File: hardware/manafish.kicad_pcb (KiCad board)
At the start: 4 copper layers, 70 x 100 mm, 103 parts, among them IC1 TPD4EUSB30, IC10 WSEN-PADS_2511020213301, IC11 BMI270, IC12 SHT45-AD1F-R2, IC2 TPD4EUSB30, IC3 JXF0-1012NL, IC4 RP2354A, IC5 Ag59824-LPB, IC6 LTV-817S, IC7 LTV-817S, IC8 LTC4162-LAD, IC9 TPSM53603RDA, J1 Conn_01x04_Pin, J2 SM03B-SRSS-TB, J3 AM32_1, J4 AM32_2, J5 Conn_01x22_Female, J6 Battery, J7 Conn_02x07_Odd_Even, J8 USB_C_Receptacle_USB2.0_14P, J9 Conn_02x08_Odd_Even, Q1 FDMC8327L, Q2 FDMC8327L, Y1 ABM8-272-T3

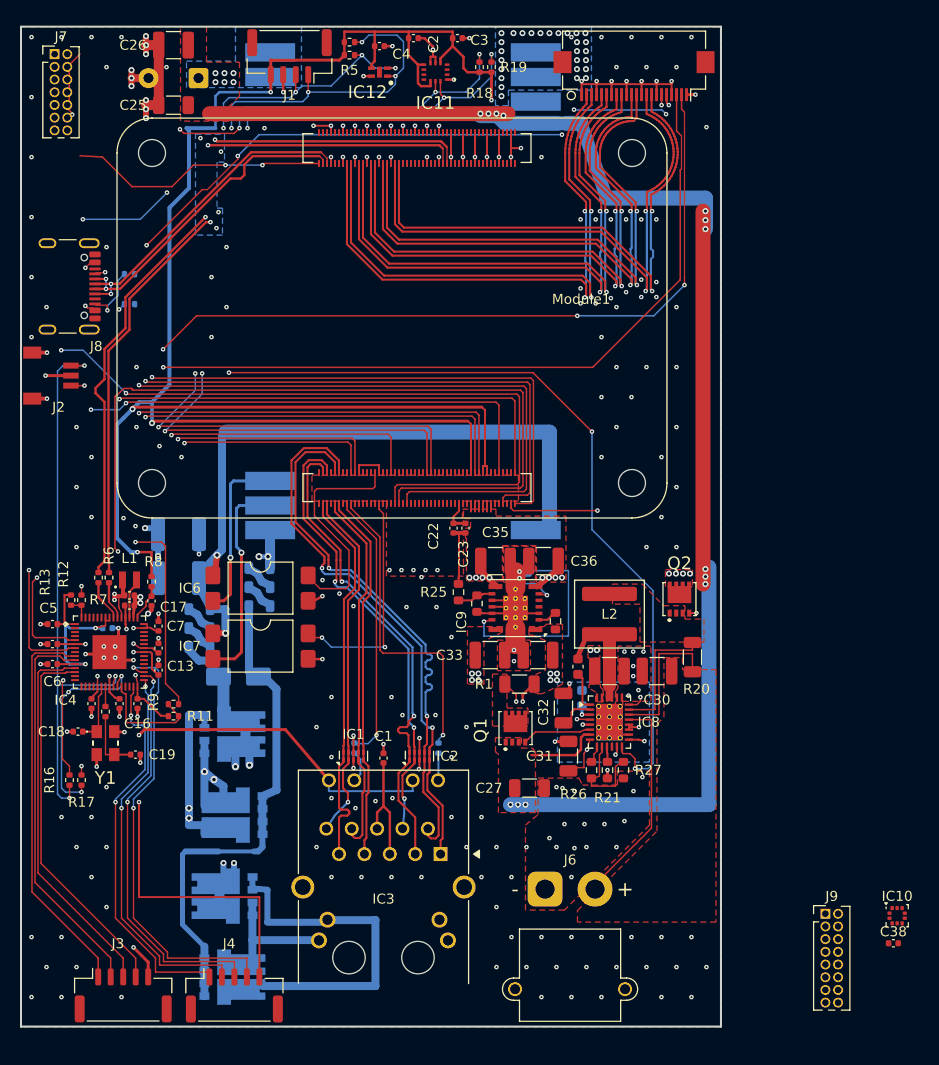
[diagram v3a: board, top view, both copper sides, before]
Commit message: Redo the PCB layout: 70 x 90 mm, power section grouped, one-side reflow
- Second camera connector J11 beside J5 on the top edge.
- SHT45 on a slotted tongue (no pour, no vias, four tracks over a 2.5 mm
  bridge) for thermal decoupling.
- All fine-pitch parts on top; the bottom holds only hand-solderable parts
  (IC5, connectors, 0603+ passives, fuses, electrolytics).
- MagJack, PoE module, charger, 5 V buck and battery connector grouped in
  the bottom half.
- Four M2 mounting holes H1-H4; silkscreen labels for the connectors and
  pin tables for J7, J9 and J13 on the bottom.
- Header pins remapped to simplify routing: J9 (CM5 GPIO), J13 (RP2354A
  GPIO22-29) and J7 (CM5 config); schematic labels updated to match.
- Default clearance 0.1 mm; DRC rules for C20's thermal, top parts under the
  CM5, IC10's land pattern and the edge parts.
- DRC: 0 errors, schematic parity clean; one expected unconnected item
  (CM5 connector-A GND pin 7, tied inside the CM5).

Co-Authored-By: Claude Opus 5.5 <noreply@anthropic.com>
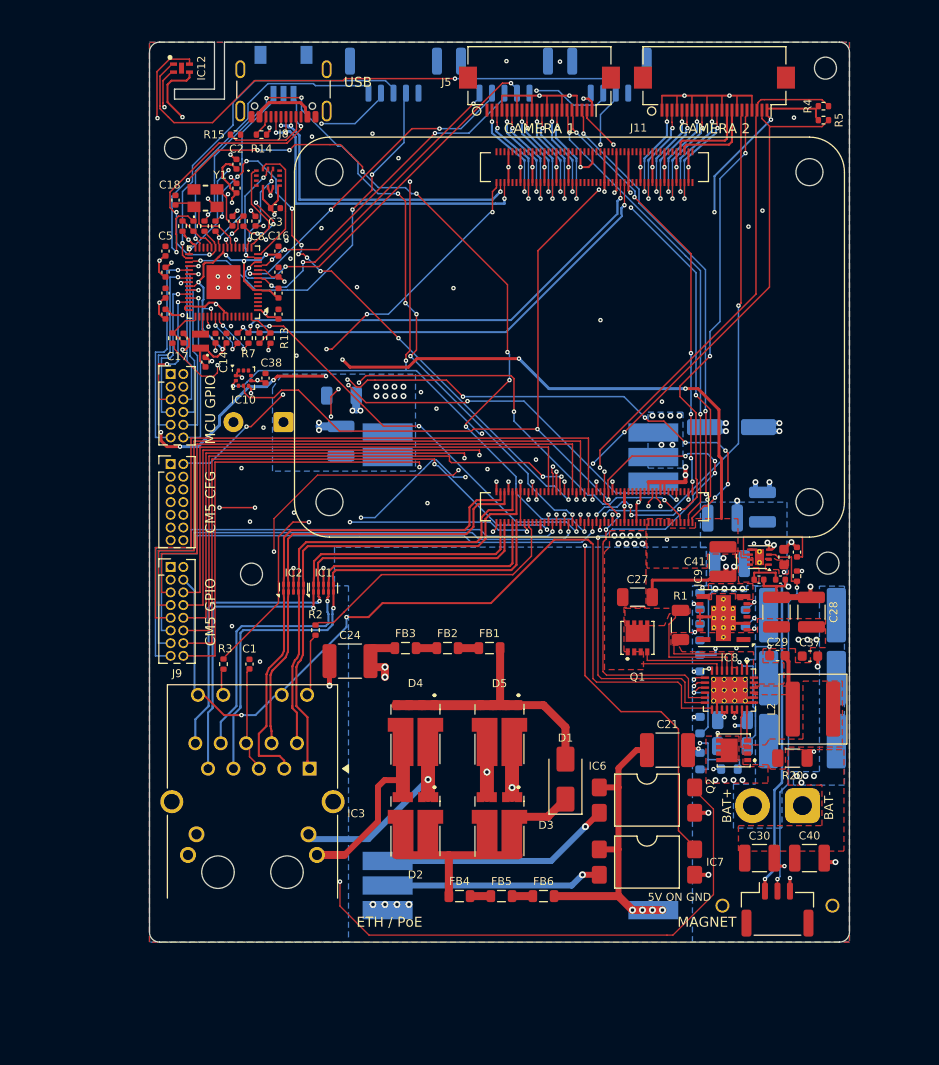
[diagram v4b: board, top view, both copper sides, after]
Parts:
- removed R18, R19: 4.7kR, Resistor_SMD:R_0402_1005Metric
- added C39: 47uF 35V, Capacitor_SMD:CP_Elec_6.3x5.8, B.Cu at (158.2, 88.5)
- added C40: 10uF 50V, Capacitor_SMD:C_1210_3225Metric, F.Cu at (166.0, 131.6)
- added C41: 47uF 10V, Capacitor_SMD:C_1210_3225Metric, F.Cu at (157.3, 102.0)
- added C47: 10uF, Capacitor_SMD:C_0603_1608Metric, F.Cu at (163.4, 101.5)
- added C48: 10nF 50V, Capacitor_SMD:C_0402_1005Metric, F.Cu at (164.8, 101.0)
- added F1: MF-LSMF260/33X-2, Fuse:Fuse_2920_7451Metric, B.Cu at (165.3, 107.3)
- added F2: MF-LSMF260/33X-2, Fuse:Fuse_2920_7451Metric, B.Cu at (165.3, 113.6)
- added F3: MF-LSMF260/33X-2, Fuse:Fuse_2920_7451Metric, B.Cu at (165.3, 119.9)
- added H1: MountingHole_2.2mm_M2, MountingHole_2.2mm_M2, F.Cu at (167.6, 52.6)
- added H2: MountingHole_2.2mm_M2, MountingHole_2.2mm_M2, F.Cu at (102.6, 60.6)
- added H3: MountingHole_2.2mm_M2, MountingHole_2.2mm_M2, F.Cu at (110.2, 103.2)
- added H4: MountingHole_2.2mm_M2, MountingHole_2.2mm_M2, F.Cu at (167.9, 102.1)
- added IC15: TPS22965DSGR, Package_SON:Texas_DSG0008A_WSON-8-1EP_2x2mm_P0.5mm_EP0.9x1.6mm_ThermalVias, F.Cu at (161.0, 101.5)
- added J11: Conn_01x22_Female, CM5IO:Hirose_FH12-22S-0.5SH_1x22-1MP_P0.50mm_Horizontal, F.Cu at (156.5, 55.0)
- added J12: Magnet, Connector_JST:JST_GH_SM03B-GHS-TB_1x03-1MP_P1.25mm_Horizontal, F.Cu at (162.8, 136.8)
- added J13: Conn_02x06_Odd_Even, Connector_PinHeader_1.27mm:PinHeader_2x06_P1.27mm_Vertical, F.Cu at (102.1, 83.2)
- added R29: 100kR, Resistor_SMD:R_0402_1005Metric, F.Cu at (164.8, 103.4)
- C11, C21, C24, C37, D1, D2, D3, D4, D5, FB1, FB2, FB3, FB4, FB5, FB6, R14, R15, R2, R3: moved to F.Cu
- C25, C26, C31, C32, C34, C35, C36, J1, J2, J3, J4, J6, R21, R22, R25, R26, R27: moved to B.Cu
- IC9: value TPSM53603RDA -> TPSM53604RDA
- R1: value 16mR -> 8mR
- R24: value 2.49kR -> 2.43kR; moved to B.Cu
- R4, R5: value 4.7kR -> 2.2kR
- moved J3 99.7 mm to (135.5, 53.2)
- moved J4 93.5 mm to (124.4, 53.2)
- moved IC10 84.6 mm to (109.4, 83.6)
- moved C38 84.5 mm to (111.6, 83.6), turned to 90 degrees
- moved J9 74.1 mm to (102.1, 102.5)
- moved R16 57.3 mm to (106.6, 68.4)
- moved R17 56.7 mm to (105.5, 68.4)
- moved Y1 55.4 mm to (105.6, 65.6), turned to 0 degrees
- moved C19 54.2 mm to (108.3, 67.9), turned to 90 degrees
- moved C18 54.0 mm to (102.6, 65.8), turned to 90 degrees
- moved C21 51.8 mm to (151.8, 120.8), turned to 0 degrees
- moved R10 51.0 mm to (109.4, 67.9)
- moved R11 49.0 mm to (103.3, 68.4), turned to 90 degrees
- moved R5 48.0 mm to (167.4, 57.8)
- moved C16 48.0 mm to (112.9, 70.9), turned to 90 degrees
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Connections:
- net /Camera Serial Interface/CAM_GPIO0 renamed /Camera Serial Interface/CAM0_GPIO0
- net /Camera Serial Interface/CAM_GPIO1 renamed /Camera Serial Interface/CAM0_GPIO1
- net /RP2354A/VREG_FB renamed /RP2354A/+1.1V
- C10 pad 1: /RP2354A/VREG_VIN -> /RP2354A/+3.3V
- C11 pad 1: /RP2354A/VREG_VIN -> /RP2354A/+3.3V
- C15 pad 1: /RP2354A/VREG_VIN -> /RP2354A/+3.3V
- C2 pad 1: /RP2354A/VREG_VIN -> /RP2354A/+3.3V
- C22 pad 1: /Power Management/+5V -> /+5V
- C23 pad 1: /Power Management/+5V -> /+5V
- C3 pad 1: /RP2354A/VREG_VIN -> /RP2354A/+3.3V
- C35 pad 1: /Power Management/+5V -> /Power Management/+5V_AON
- C36 pad 1: /Power Management/+5V -> /Power Management/+5V_AON
- C38 pad 1: /RP2354A/VREG_VIN -> /RP2354A/+3.3V
- C4 pad 1: /RP2354A/VREG_VIN -> /RP2354A/+3.3V
- C5 pad 1: /RP2354A/VREG_VIN -> /RP2354A/+3.3V
- C6 pad 1: /RP2354A/VREG_VIN -> /RP2354A/+3.3V
- C7 pad 1: /RP2354A/VREG_VIN -> /RP2354A/+3.3V
- C8 pad 1: /RP2354A/VREG_VIN -> /RP2354A/+3.3V
- C9 pad 1: /RP2354A/VREG_VIN -> /RP2354A/+3.3V
- IC10 pad 1: /RP2354A/VREG_VIN -> /RP2354A/+3.3V
- IC10 pad 10: /RP2354A/VREG_VIN -> /RP2354A/+3.3V
- IC10 pad 2: /I2C Peripherals/I2C1_SCL -> /Power Management/I2C1_SCL
- IC10 pad 4: /I2C Peripherals/I2C1_SDA -> /Power Management/I2C1_SDA
- IC10 pad 5: unconnected-(U10-SA0-Pad5) -> GND
- IC10 pad 6: unconnected-(U10-~{CS}-Pad6) -> /RP2354A/+3.3V
- IC10 pad 7: /I2C Peripherals/INT_DRDY -> unconnected-(IC10-INT_DRDY-Pad7)
- IC11 pad 1: GND -> /RP2354A/MISO
- IC11 pad 12: /RP2354A/VREG_VIN -> /RP2354A/CS
- IC11 pad 13: /I2C Peripherals/I2C0_SCL -> /RP2354A/SCK
- IC11 pad 14: /I2C Peripherals/I2C0_SDA -> /RP2354A/MOSI
- IC11 pad 5: /RP2354A/VREG_VIN -> /RP2354A/+3.3V
- IC11 pad 8: /RP2354A/VREG_VIN -> /RP2354A/+3.3V
- IC12 pad 1: /I2C Peripherals/I2C1_SDA -> /Power Management/I2C1_SDA
- IC12 pad 2: /I2C Peripherals/I2C1_SCL -> /Power Management/I2C1_SCL
- IC12 pad 3: /RP2354A/VREG_VIN -> /RP2354A/+3.3V
- IC3 pad 11: /RP2354A/VREG_VIN -> /RP2354A/+3.3V
- IC3 pad 13: /RP2354A/VREG_VIN -> /RP2354A/+3.3V
- IC4 pad 1: /RP2354A/VREG_VIN -> /RP2354A/+3.3V
- IC4 pad 11: /RP2354A/VREG_VIN -> /RP2354A/+3.3V
- IC4 pad 14: unconnected-(U4-GPIO10-Pad14) -> /RP2354A/SCK
- IC4 pad 15: unconnected-(U4-GPIO11-Pad15) -> /RP2354A/MOSI
- IC4 pad 16: unconnected-(U4-GPIO12-Pad16) -> /RP2354A/MISO
- IC4 pad 17: unconnected-(U4-GPIO13-Pad17) -> /RP2354A/CS
- IC4 pad 20: /RP2354A/VREG_VIN -> /RP2354A/+3.3V
- IC4 pad 30: /RP2354A/VREG_VIN -> /RP2354A/+3.3V
- IC4 pad 34: unconnected-(U4-GPIO22-Pad34) -> /RP2354A/GPIO22
- IC4 pad 35: unconnected-(U4-GPIO23-Pad35) -> /RP2354A/GPIO23
- IC4 pad 36: unconnected-(U4-GPIO24-Pad36) -> /RP2354A/GPIO24
- IC4 pad 37: unconnected-(U4-GPIO25-Pad37) -> /RP2354A/GPIO25
- IC4 pad 38: /RP2354A/VREG_VIN -> /RP2354A/+3.3V
- IC4 pad 40: unconnected-(U4-GPIO26/ADC0-Pad40) -> /RP2354A/GPIO26
- IC4 pad 41: unconnected-(U4-GPIO27/ADC1-Pad41) -> /RP2354A/GPIO27
- IC4 pad 42: unconnected-(U4-GPIO28/ADC2-Pad42) -> /RP2354A/GPIO28
- IC4 pad 43: unconnected-(U4-GPIO29/ADC3-Pad43) -> /RP2354A/GPIO29
- IC4 pad 44: /RP2354A/VREG_VIN -> /RP2354A/+3.3V
- IC4 pad 45: /RP2354A/VREG_VIN -> /RP2354A/+3.3V
- IC4 pad 49: /RP2354A/VREG_VIN -> /RP2354A/+3.3V
- IC4 pad 5: /I2C Peripherals/I2C0_SCL -> unconnected-(IC4-GPIO3-Pad5)
- IC4 pad 53: /RP2354A/VREG_VIN -> /RP2354A/+3.3V
- IC4 pad 54: /RP2354A/VREG_VIN -> /RP2354A/+3.3V
- IC4 pad 7: /I2C Peripherals/I2C0_SDA -> unconnected-(IC4-GPIO4-Pad7)
- IC8 pad 13: /I2C Peripherals/I2C1_SCL -> /Power Management/I2C1_SCL
- IC8 pad 14: /I2C Peripherals/I2C1_SDA -> /Power Management/I2C1_SDA
- IC8 pad 15: /RP2354A/VREG_VIN -> /RP2354A/+3.3V
- IC9 pad 7: /Power Management/+5V -> /Power Management/+5V_AON
- IC9 pad 8: /Power Management/+5V -> /Power Management/+5V_AON
- J1 pad 1: /I2C Peripherals/I2C1_SDA -> /RP2354A/+3.3V
- J1 pad 2: /I2C Peripherals/I2C1_SCL -> /Power Management/I2C1_SCL
- J1 pad 3: GND -> /Power Management/I2C1_SDA
- J1 pad 4: /RP2354A/VREG_VIN -> GND
- J5 pad 22: /RP2354A/VREG_VIN -> /RP2354A/+3.3V
- J6 pad 2: /Power Management/BAT+ -> /BAT_IN
- J7 pad 10: /Rasperry Pi Compute Module 5/USBOTG -> /Rasperry Pi Compute Module 5/nRPIBOOT
- J7 pad 12: /Rasperry Pi Compute Module 5/PMIC_ENABLE -> /Rasperry Pi Compute Module 5/EEPROM_nWP
- J7 pad 14: /Rasperry Pi Compute Module 5/PWR_BUT -> /Rasperry Pi Compute Module 5/SYNC_OUT
- J7 pad 2: /Rasperry Pi Compute Module 5/nRPIBOOT -> /Rasperry Pi Compute Module 5/USBOTG
- J7 pad 4: /Rasperry Pi Compute Module 5/EEPROM_nWP -> /Rasperry Pi Compute Module 5/PWR_BUT
- J7 pad 6: /Rasperry Pi Compute Module 5/SYNC_OUT -> /Rasperry Pi Compute Module 5/PMIC_ENABLE
- J9 pad 1: /Rasperry Pi Compute Module 5/GPIO21 -> /+5V
- J9 pad 11: /Rasperry Pi Compute Module 5/GPIO23 -> /Rasperry Pi Compute Module 5/GPIO18
- J9 pad 12: /Rasperry Pi Compute Module 5/GPIO27 -> /Rasperry Pi Compute Module 5/GPIO5
- J9 pad 13: /Rasperry Pi Compute Module 5/GPIO18 -> /Rasperry Pi Compute Module 5/GPIO7
- J9 pad 14: /Rasperry Pi Compute Module 5/GPIO17 -> /Rasperry Pi Compute Module 5/GPIO23
- J9 pad 15: /Rasperry Pi Compute Module 5/GPIO15 -> /Rasperry Pi Compute Module 5/GPIO16
- J9 pad 16: /Rasperry Pi Compute Module 5/GPIO4 -> /Rasperry Pi Compute Module 5/GPIO20
- J9 pad 2: /Rasperry Pi Compute Module 5/GPIO19 -> GND
- J9 pad 3: /Rasperry Pi Compute Module 5/GPIO20 -> GND
- J9 pad 4: /Rasperry Pi Compute Module 5/GPIO13 -> /RP2354A/+3.3V
- J9 pad 5: /Rasperry Pi Compute Module 5/GPIO16 -> /Rasperry Pi Compute Module 5/GPIO9
- J9 pad 6: /Rasperry Pi Compute Module 5/GPIO5 -> /Rasperry Pi Compute Module 5/GPIO13
- J9 pad 7: /Rasperry Pi Compute Module 5/GPIO7 -> /Rasperry Pi Compute Module 5/GPIO10
- J9 pad 8: /Rasperry Pi Compute Module 5/GPIO9 -> /Rasperry Pi Compute Module 5/GPIO17
- J9 pad 9: /Rasperry Pi Compute Module 5/GPIO10 -> /Rasperry Pi Compute Module 5/GPIO27
- Module1 pad 175: unconnected-(Module1B-MIPI1_D0_N-Pad175) -> /Camera Serial Interface/DPHY1_D0_N
- Module1 pad 177: unconnected-(Module1B-MIPI1_D0_P-Pad177) -> /Camera Serial Interface/DPHY1_D0_P
- Module1 pad 181: unconnected-(Module1B-MIPI1_D1_N-Pad181) -> /Camera Serial Interface/DPHY1_D1_N
- Module1 pad 183: unconnected-(Module1B-MIPI1_D1_P-Pad183) -> /Camera Serial Interface/DPHY1_D1_P
- Module1 pad 187: unconnected-(Module1B-MIPI1_C_N-Pad187) -> /Camera Serial Interface/DPHY1_C_N
- Module1 pad 189: unconnected-(Module1B-MIPI1_C_P-Pad189) -> /Camera Serial Interface/DPHY1_C_P
- Module1 pad 193: unconnected-(Module1B-MIPI1_D2_N-Pad193) -> /Camera Serial Interface/DPHY1_D2_N
- Module1 pad 194: unconnected-(Module1B-MIPI1_D3_N-Pad194) -> /Camera Serial Interface/DPHY1_D3_N
- Module1 pad 195: unconnected-(Module1B-MIPI1_D2_P-Pad195) -> /Camera Serial Interface/DPHY1_D2_P
- Module1 pad 196: unconnected-(Module1B-MIPI1_D3_P-Pad196) -> /Camera Serial Interface/DPHY1_D3_P
- Module1 pad 24: /I2C Peripherals/INT_DRDY -> unconnected-(Module1A-GPIO26-Pad24)
- Module1 pad 25: /Rasperry Pi Compute Module 5/GPIO21 -> unconnected-(Module1A-GPIO21-Pad25)
- Module1 pad 26: /Rasperry Pi Compute Module 5/GPIO19 -> unconnected-(Module1A-GPIO19-Pad26)
- Module1 pad 35: unconnected-(Module1A-ID_SC-Pad35) -> /Camera Serial Interface/SCL1
- Module1 pad 36: unconnected-(Module1A-ID_SD-Pad36) -> /Camera Serial Interface/SDA1
- Module1 pad 51: /Rasperry Pi Compute Module 5/GPIO15 -> /Camera Serial Interface/CAM1_GPIO1
- Module1 pad 54: /Rasperry Pi Compute Module 5/GPIO4 -> unconnected-(Module1A-GPIO4-Pad54)
- Module1 pad 55: unconnected-(Module1A-GPIO14-Pad55) -> /Camera Serial Interface/CAM1_GPIO0
- Module1 pad 56: /I2C Peripherals/I2C1_SCL -> /Power Management/I2C1_SCL
- Module1 pad 58: /I2C Peripherals/I2C1_SDA -> /Power Management/I2C1_SDA
- Module1 pad 77: /Power Management/+5V -> /+5V
- Module1 pad 78: /RP2354A/VREG_VIN -> /RP2354A/+3.3V
- Module1 pad 79: /Power Management/+5V -> /+5V
- Module1 pad 81: /Power Management/+5V -> /+5V
- Module1 pad 83: /Power Management/+5V -> /+5V
- Module1 pad 84: /RP2354A/VREG_VIN -> /RP2354A/+3.3V
- Module1 pad 85: /Power Management/+5V -> /+5V
- Module1 pad 86: /RP2354A/VREG_VIN -> /RP2354A/+3.3V
- Module1 pad 87: /Power Management/+5V -> /+5V
- R11 pad 1: /RP2354A/VREG_VIN -> /RP2354A/+3.3V
- R13 pad 1: /RP2354A/VREG_VIN -> /RP2354A/+3.3V
- R25 pad 1: /Power Management/+5V -> /Power Management/+5V_AON
- R4 pad 1: /RP2354A/VREG_VIN -> /RP2354A/+3.3V
- R4 pad 2: /I2C Peripherals/I2C1_SCL -> /Camera Serial Interface/SCL1
- R5 pad 1: /RP2354A/VREG_VIN -> /RP2354A/+3.3V
- R5 pad 2: /I2C Peripherals/I2C1_SDA -> /Camera Serial Interface/SDA1
- R8 pad 1: /RP2354A/VREG_VIN -> /RP2354A/+3.3V
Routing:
- net /RP2354A/VREG_VIN: track 316.9 -> 0.00 mm, vias 16 -> 0
- net /I2C Peripherals/I2C1_SCL: track 199.9 -> 0.00 mm, vias 9 -> 0
- net /RP2354A/+3.3V: track 0.00 -> 194.1 mm, vias 0 -> 25
- net /Power Management/I2C1_SDA: track 0.00 -> 186.0 mm, vias 0 -> 9
- net /I2C Peripherals/I2C1_SDA: track 183.1 -> 0.00 mm, vias 9 -> 0
- net /Power Management/I2C1_SCL: track 0.00 -> 152.4 mm, vias 0 -> 9
- net /Power Management/24V: track 149.4 -> 7.94 mm, vias 19 -> 16
- net /I2C Peripherals/I2C0_SDA: track 117.1 -> 0.00 mm, vias 4 -> 0
- net /Power Management/POE_TYP2_DET: track 22.4 -> 127.2 mm, vias 0 -> 4
- net /I2C Peripherals/I2C0_SCL: track 102.3 -> 0.00 mm, vias 7 -> 0
- net /+5V: track 0.00 -> 100.0 mm, vias 0 -> 7
- net /Camera Serial Interface/CAM0_GPIO1: track 125.1 -> 42.2 mm, vias 5 -> 6
- net /Camera Serial Interface/SDA0: track 121.5 -> 49.9 mm, vias 4 -> 5
- net /Rasperry Pi Compute Module 5/GPIO27: track 0.00 -> 68.1 mm
- net /Camera Serial Interface/SCL0: track 118.3 -> 50.4 mm, vias 2 -> 4
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- added copper zone on F.Cu, net /+5V
- added copper zone on B.Cu, net /BAT_IN
- added copper zone on B.Cu, net /Power Management/+5V_AON
- added copper zone on F.Cu, net /Power Management/+5V_AON
- added copper zone on In2.Cu, net /Power Management/24V
- added copper zone on B.Cu, net /Power Management/BAT+
- added copper zone on In2.Cu, net /RP2354A/+3.3V
- added copper zone on F.Cu, net Net-(C29-Pad2)
- removed copper zone on F.Cu, net /Power Management/+5V
- removed copper zone on In2.Cu, net /Power Management/+5V
- removed copper zone on In2.Cu, net /RP2354A/VREG_VIN
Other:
- board size 70 x 100 mm -> 70 x 90 mm
- board text added: "1 5V"
- board text added: "1 GND"
- board text added: "10 GP26"
- board text added: "10 IO22"
- board text added: "10 nRPIBOOT"
- board text added: "11 GND"
- board text added: "11 GP23"
- board text added: "11 IO18"
- board text added: "12 EE_nWP"
- board text added: "12 GP28"
- board text added: "12 IO5"
- board text added: "13 GND"
- board text added: "13 IO7"
- board text added: "14 IO23"
- board text added: "14 SYNC_OUT"
- board text added: "15 IO16"
- board text added: "16 IO20"
- board text added: "2 GND"
- board text added: "2 USBOTG"
- board text added: "3 GND"
- board text added: "4 3V3"
- board text added: "4 PWR_BUT"
- board text added: "5 GND"
- board text added: "5 GP29"
- board text added: "5 IO9"
- board text added: "5V ON GND"
- board text added: "6 GP22"
- board text added: "6 IO13"
- board text added: "6 PMIC_EN"
- board text added: "7 GND"
- board text added: "7 GP27"
- board text added: "7 IO10"
- board text added: "8 GP24"
- board text added: "8 IO17"
- board text added: "8 NC"
- board text added: "9 GND"
- board text added: "9 GP25"
- board text added: "9 IO27"
- board text added: "BAT+"
- board text added: "BAT-"
- board text added: "BATTERY"
- board text added: "CAMERA 1"
- board text added: "CAMERA 2"
- board text added: "CM5 CFG"
- board text added: "CM5 GPIO"
- board text added: "ESC 1"
- board text added: "ESC 2"
- board text added: "ETH / PoE"
- board text added: "ETHERNET / PoE"
- board text added: "FABRICATION JLCPCB 4 layers, 1.6 mm, stackup JLC04161H-7628, 1 oz outer / 0.5 oz inner, ENIG. Board 70 x 90 mm. Vias tented; open vias: the 4 exposed-pad vias of IC4 (in the gaps of its paste grid), the thermal vias of IC8 and IC9, and the vias in the bottom pads of IC5 (VIN+/VIN-) and C31 (hand-soldered). Impedance control +-10 %: L1/L4 100 ohm differential, 0.21 mm / 0.19 mm gap (Ethernet TRD*,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"
- board text added: "J13 MCU GPIO"
- board text added: "J7 CM5 CFG"
- board text added: "J9 CM5 GPIO"
- board text added: "MAGNET"
- board text added: "MANAFISH MAINBOARD"
- board text added: "MCU GPIO"
- board text added: "MS5837"
- board text added: "SWD"
- board text added: "USB"
- board text added: "rev 2 - 2026-10"
- board text removed: "FABRICATION JLCPCB 4 layers, 1.6 mm, stackup JLC04161H-7628, 1 oz outer / 0.5 oz inner, ENIG. Vias tented; the exposed-pad vias of IC4, IC8 and IC9 stay open (their paste windows keep clear of the holes). Impedance control +-10 %: L1/L4 100 ohm differential, 0.21 mm / 0.19 mm gap (Ethernet TRD*, CSI DPHY0_*); L1 90 ohm differential, 0.24 mm / 0.15 mm gap (USB). Min track 0.1 mm, min via 0.45/0.2 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"
